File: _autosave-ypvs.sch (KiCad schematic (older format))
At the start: 22 parts, among them J1 Servo, J2 LM_2596 _Input, J3 HV_Cable, J4 Motorcycle Battery, U1 Stm32f103_BluePill, U2 LM1117-3.3, U3 H11L1

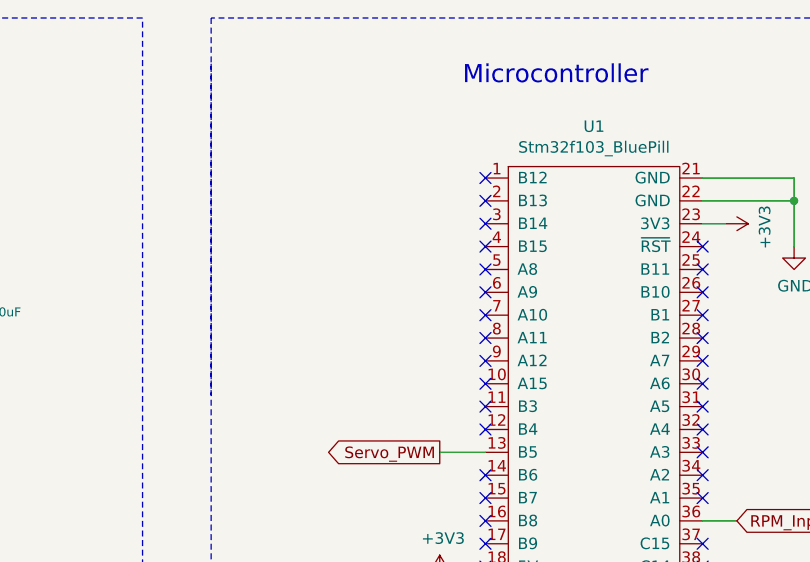
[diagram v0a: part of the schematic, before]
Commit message: Added PCB traces
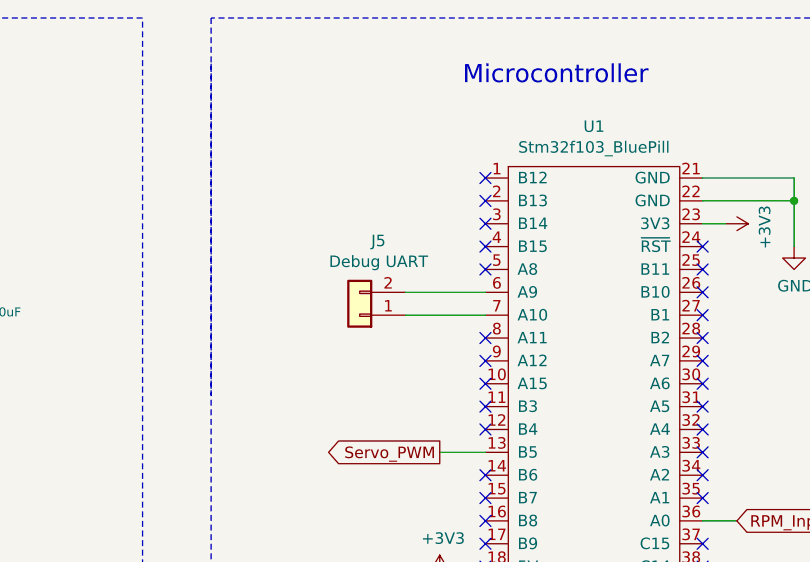
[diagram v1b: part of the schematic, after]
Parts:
- added J5: Debug UART, Connector_PinHeader_2.54mm:PinHeader_1x02_P2.54mm_Vertical, symbol Connector_Generic:Conn_01x02
- D3: footprint (none) -> Diode_THT:D_A-405_P7.62mm_Horizontal
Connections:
- net at U1.6 (A9): now also J5.2 (Pin_2)
- net at U1.7 (A10): now also J5.1 (Pin_1)
- no-connect marks 34 -> 32
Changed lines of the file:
@@
 Wire Wire Line
 	1250 5500 1350 5500
-$Comp
-L Ypvs:Stm32f103_BluePill U1
-U 1 1 5F48EF1D
-P 6050 2250
-F 0 "U1" H 6025 3375 50  0000 C CNN
-F 1 "Stm32f103_BluePill" H 6025 3284 50  0000 C CNN
-F 2 "Package_DIP:DIP-40_W15.24mm_LongPads" H 6000 2200 50  0001 C CNN
-F 3 "" H 6000 2200 50  0001 C CNN
-	1    6050 2250
-	1    0    0    -1
-$EndComp
 Text GLabel 6650 2850 2    50   Input ~ 0
 RPM_Input
@@
 NoConn ~ 5550 1650
 NoConn ~ 5550 1750
-NoConn ~ 5550 1850
-NoConn ~ 5550 1950
 NoConn ~ 5550 2050
 NoConn ~ 5550 2150
@@
 F 0 "D3" H 1650 3367 50  0000 C CNN
 F 1 "1N4001" H 1650 3276 50  0000 C CNN
-F 2 "" H 1650 3150 50  0001 C CNN
+F 2 "Diode_THT:D_A-405_P7.62mm_Horizontal" H 1650 3150 50  0001 C CNN
 F 3 "~" H 1650 3150 50  0001 C CNN
 	1    1650 3150
@@
 Wire Wire Line
 	1500 3150 1400 3150
+$Comp
+L Connector_Generic:Conn_01x02 J5
+U 1 1 5F521F21
+P 5000 1950
+F 0 "J5" H 4918 1625 50  0000 C CNN
+F 1 "Debug UART" H 4918 1716 50  0000 C CNN
+F 2 "Connector_PinHeader_2.54mm:PinHeader_1x02_P2.54mm_Vertical" H 5000 1950 50  0001 C CNN
+F 3 "~" H 5000 1950 50  0001 C CNN
+	1    5000 1950
+	-1   0    0    1
+$EndComp
+$Comp
+L Ypvs:Stm32f103_BluePill U1
+U 1 1 5F48EF1D
+P 6050 2250
+F 0 "U1" H 6025 3375 50  0000 C CNN
+F 1 "Stm32f103_BluePill" H 6025 3284 50  0000 C CNN
+F 2 "Package_DIP:DIP-40_W15.24mm_LongPads" H 6000 2200 50  0001 C CNN
+F 3 "" H 6000 2200 50  0001 C CNN
+	1    6050 2250
+	1    0    0    -1
+$EndComp
+Wire Wire Line
+	5200 1850 5550 1850
+Wire Wire Line
+	5200 1950 5550 1950
 $EndSCHEMATC
